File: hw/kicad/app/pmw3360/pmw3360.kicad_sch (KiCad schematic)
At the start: 2 parts, among them J2 TOP, J4 BUTTOM

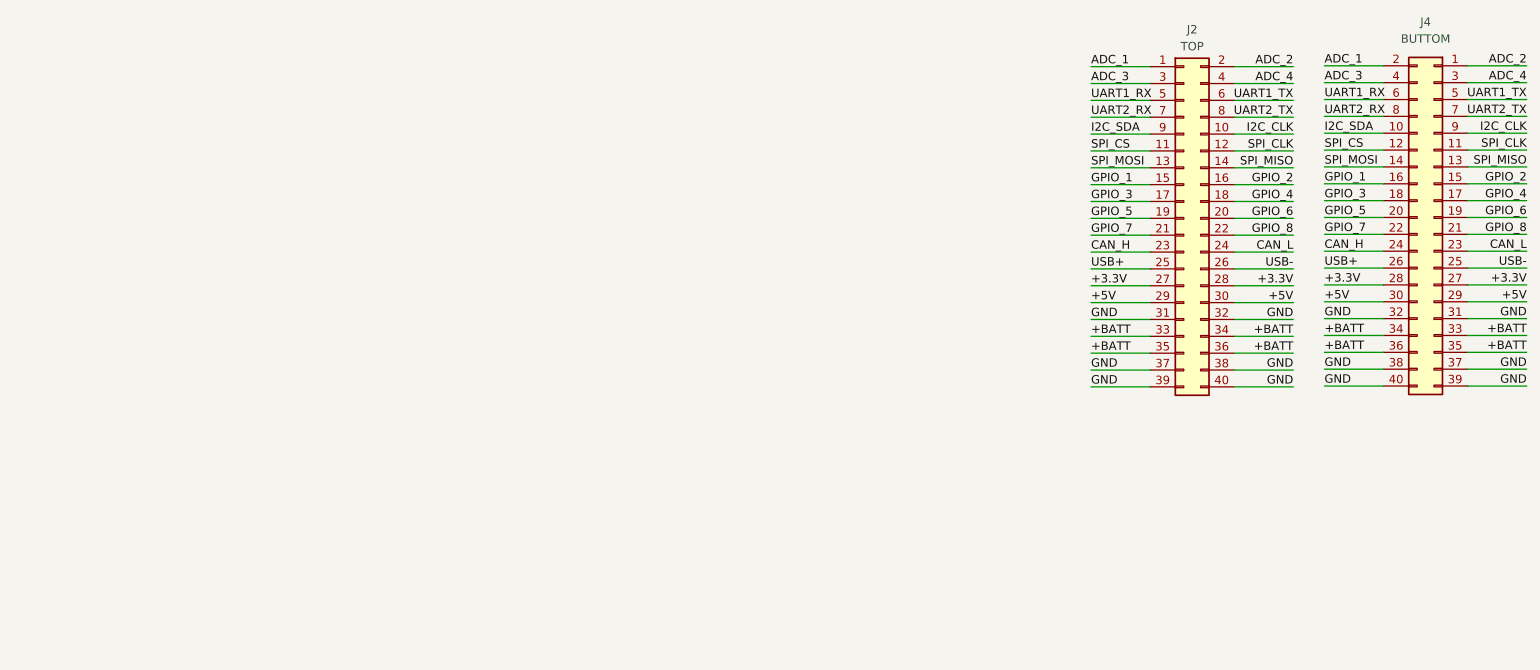
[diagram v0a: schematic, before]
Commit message: 新增陀螺仪小板子
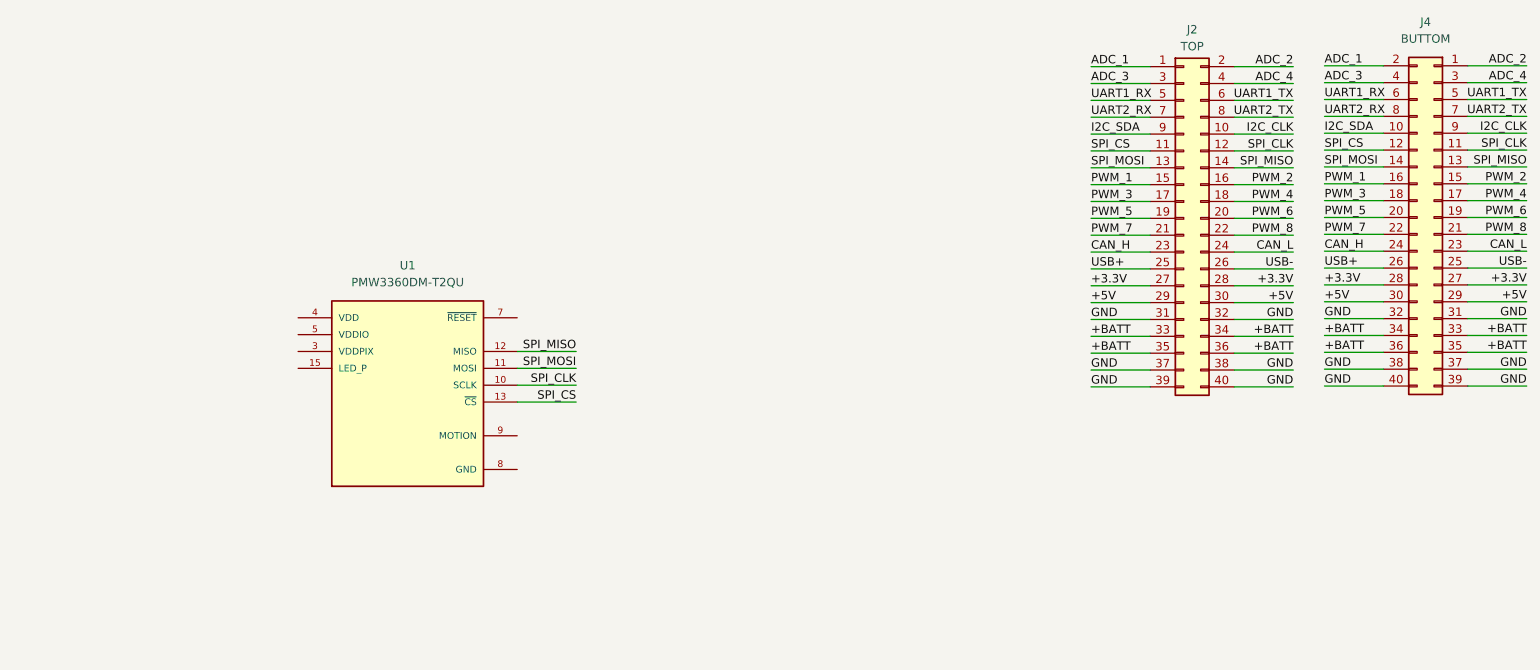
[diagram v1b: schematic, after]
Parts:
- added U1: PMW3360DM-T2QU, symbol PMW3360DM:PMW3360DM-T2QU
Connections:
- net SPI_CLK: now also U1.10 (SCLK)
- net SPI_CS: now also U1.13 (~{CS})
- net SPI_MISO: now also U1.12 (MISO)
- net SPI_MOSI: now also U1.11 (MOSI)
- net GPIO_1 renamed PWM_1
- net GPIO_2 renamed PWM_2
- net GPIO_3 renamed PWM_3
- net GPIO_4 renamed PWM_4
- net GPIO_5 renamed PWM_5
- net GPIO_6 renamed PWM_6
- net GPIO_7 renamed PWM_7
- net GPIO_8 renamed PWM_8
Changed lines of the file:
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@@
+    (stroke (width 0) (type default))
+  )
+  (wire (pts (xy 128.143 84.074) (xy 119.253 84.074))
     (stroke (width 0) (type default))
   )
@@
     (stroke (width 0) (type default))
   )
+  (wire (pts (xy 128.143 89.154) (xy 119.253 89.154))
+    (stroke (width 0) (type default))
+  )
   (wire (pts (xy 271.399 56.261) (xy 262.509 56.261))
     (stroke (width 0) (type default))
   )
+  (wire (pts (xy 128.143 91.694) (xy 119.253 91.694))
+    (stroke (width 0) (type default))
+  )
   (wire (pts (xy 240.919 76.581) (xy 249.809 76.581))
     (stroke (width 0) (type default))
@@
     (stroke (width 0) (type default))
   )
+  (wire (pts (xy 128.143 86.614) (xy 119.253 86.614))
+    (stroke (width 0) (type default))
+  )
   (wire (pts (xy 240.919 89.281) (xy 249.809 89.281))
     (stroke (width 0) (type default))
@@
     (effects (font (size 1.27 1.27)) (justify right bottom))
   )
+  (label "SPI_MISO" (at 128.143 84.074 180) (fields_autoplaced)
+    (effects (font (size 1.27 1.27)) (justify right bottom))
+  )
   (label "I2C_SDA" (at 205.74 51.308 0) (fields_autoplaced)
     (effects (font (size 1.27 1.27)) (justify left bottom))
   )
-  (label "GPIO_5" (at 240.919 63.881 0) (fields_autoplaced)
-    (effects (font (size 1.27 1.27)) (justify left bottom))
-  )
-  (label "GPIO_3" (at 240.919 61.341 0) (fields_autoplaced)
+  (label "PWM_5" (at 240.919 63.881 0) (fields_autoplaced)
+    (effects (font (size 1.27 1.27)) (justify left bottom))
+  )
+  (label "PWM_3" (at 240.919 61.341 0) (fields_autoplaced)
     (effects (font (size 1.27 1.27)) (justify left bottom))
   )
@@
     (effects (font (size 1.27 1.27)) (justify right bottom))
   )
-  (label "GPIO_4" (at 271.399 61.341 180) (fields_autoplaced)
-    (effects (font (size 1.27 1.27)) (justify right bottom))
-  )
-  (label "GPIO_3" (at 205.74 61.468 0) (fields_autoplaced)
+  (label "PWM_4" (at 271.399 61.341 180) (fields_autoplaced)
+    (effects (font (size 1.27 1.27)) (justify right bottom))
+  )
+  (label "PWM_3" (at 205.74 61.468 0) (fields_autoplaced)
     (effects (font (size 1.27 1.27)) (justify left bottom))
   )
@@
     (effects (font (size 1.27 1.27)) (justify left bottom))
   )
-  (label "GPIO_6" (at 271.399 63.881 180) (fields_autoplaced)
+  (label "PWM_6" (at 271.399 63.881 180) (fields_autoplaced)
     (effects (font (size 1.27 1.27)) (justify right bottom))
   )
@@
     (effects (font (size 1.27 1.27)) (justify right bottom))
   )
-  (label "GPIO_1" (at 240.919 58.801 0) (fields_autoplaced)
-    (effects (font (size 1.27 1.27)) (justify left bottom))
-  )
-  (label "GPIO_2" (at 271.399 58.801 180) (fields_autoplaced)
+  (label "PWM_1" (at 240.919 58.801 0) (fields_autoplaced)
+    (effects (font (size 1.27 1.27)) (justify left bottom))
+  )
+  (label "SPI_CLK" (at 128.143 89.154 180) (fields_autoplaced)
+    (effects (font (size 1.27 1.27)) (justify right bottom))
+  )
+  (label "PWM_2" (at 271.399 58.801 180) (fields_autoplaced)
     (effects (font (size 1.27 1.27)) (justify right bottom))
   )
@@
     (effects (font (size 1.27 1.27)) (justify right bottom))
   )
-  (label "GPIO_7" (at 240.919 66.421 0) (fields_autoplaced)
-    (effects (font (size 1.27 1.27)) (justify left bottom))
-  )
-  (label "GPIO_8" (at 236.22 66.548 180) (fields_autoplaced)
+  (label "PWM_7" (at 240.919 66.421 0) (fields_autoplaced)
+    (effects (font (size 1.27 1.27)) (justify left bottom))
+  )
+  (label "PWM_8" (at 236.22 66.548 180) (fields_autoplaced)
     (effects (font (size 1.27 1.27)) (justify right bottom))
   )
@@
     (effects (font (size 1.27 1.27)) (justify right bottom))
   )
-  (label "GPIO_7" (at 205.74 66.548 0) (fields_autoplaced)
+  (label "PWM_7" (at 205.74 66.548 0) (fields_autoplaced)
     (effects (font (size 1.27 1.27)) (justify left bottom))
   )
@@
     (effects (font (size 1.27 1.27)) (justify right bottom))
   )
-  (label "GPIO_6" (at 236.22 64.008 180) (fields_autoplaced)
+  (label "PWM_6" (at 236.22 64.008 180) (fields_autoplaced)
     (effects (font (size 1.27 1.27)) (justify right bottom))
   )
@@
     (effects (font (size 1.27 1.27)) (justify right bottom))
   )
-  (label "GPIO_5" (at 205.74 64.008 0) (fields_autoplaced)
-    (effects (font (size 1.27 1.27)) (justify left bottom))
-  )
-  (label "GPIO_4" (at 236.22 61.468 180) (fields_autoplaced)
-    (effects (font (size 1.27 1.27)) (justify right bottom))
-  )
-  (label "GPIO_1" (at 205.74 58.928 0) (fields_autoplaced)
+  (label "PWM_5" (at 205.74 64.008 0) (fields_autoplaced)
+    (effects (font (size 1.27 1.27)) (justify left bottom))
+  )
+  (label "SPI_CS" (at 128.143 91.694 180) (fields_autoplaced)
+    (effects (font (size 1.27 1.27)) (justify right bottom))
+  )
+  (label "PWM_4" (at 236.22 61.468 180) (fields_autoplaced)
+    (effects (font (size 1.27 1.27)) (justify right bottom))
+  )
+  (label "PWM_1" (at 205.74 58.928 0) (fields_autoplaced)
     (effects (font (size 1.27 1.27)) (justify left bottom))
   )
@@
     (effects (font (size 1.27 1.27)) (justify right bottom))
   )
-  (label "GPIO_2" (at 236.22 58.928 180) (fields_autoplaced)
+  (label "PWM_2" (at 236.22 58.928 180) (fields_autoplaced)
     (effects (font (size 1.27 1.27)) (justify right bottom))
   )
@@
     (effects (font (size 1.27 1.27)) (justify left bottom))
   )
+  (label "SPI_MOSI" (at 128.143 86.614 180) (fields_autoplaced)
+    (effects (font (size 1.27 1.27)) (justify right bottom))
+  )
   (label "GND" (at 240.919 86.741 0) (fields_autoplaced)
     (effects (font (size 1.27 1.27)) (justify left bottom))
@@
     (effects (font (size 1.27 1.27)) (justify right bottom))
   )
-  (label "GPIO_8" (at 271.399 66.421 180) (fields_autoplaced)
+  (label "PWM_8" (at 271.399 66.421 180) (fields_autoplaced)
     (effects (font (size 1.27 1.27)) (justify right bottom))
   )
@@
     (pin "9")
     (instances
-      (project "tamplate"
+      (project "pmw3360"
         (path "/988ee502-8596-4ebe-9b99-0eb76e7d156a"
           (reference "J4") (unit 1)
+        )
+      )
+    )
+  )
+  (symbol (lib_id "PMW3360DM:PMW3360DM-T2QU") (at 104.013 89.154 0) (unit 1)
+    (in_bom yes) (on_board yes) (dnp no) (fields_autoplaced)
+    (property "Reference" "U1" (at 102.743 71.12 0)
+      (effects (font (size 1.27 1.27)))
+    )
+    (property "Value" "PMW3360DM-T2QU" (at 102.743 73.66 0)
+      (effects (font (size 1.27 1.27)))
+    )
+    (property "Footprint" "" (at 104.013 89.154 0)
+      (effects (font (size 1.27 1.27)) hide)
+    )
+    (property "Datasheet" "" (at 104.013 89.154 0)
+      (effects (font (size 1.27 1.27)) hide)
+    )
+    (property "MANUFACTURER_NAME" "PixArt Imaging Inc." (at 104.013 89.154 0)
+      (effects (font (size 1.27 1.27)) (justify bottom) hide)
+    )
+    (property "MOUSER_PRICE-STOCK" "" (at 104.013 89.154 0)
+      (effects (font (size 1.27 1.27)) (justify bottom) hide)
+    )
+    (property "DESCRIPTION" "Optical gaming navigation sensor" (at 104.013 89.154 0)
+      (effects (font (size 1.27 1.27)) (justify bottom) hide)
+    )
+    (property "MOUSER_PART_NUMBER" "" (at 104.013 89.154 0)
+      (effects (font (size 1.27 1.27)) (justify bottom) hide)
+    )
+    (property "HEIGHT" "mm" (at 104.013 89.154 0)
+      (effects (font (size 1.27 1.27)) (justify bottom) hide)
+    )
+    (property "ARROW_PRICE-STOCK" "" (at 104.013 89.154 0)
+      (effects (font (size 1.27 1.27)) (justify bottom) hide)
+    )
+    (property "ARROW_PART_NUMBER" "" (at 104.013 89.154 0)
+      (effects (font (size 1.27 1.27)) (justify bottom) hide)
+    )
+    (property "MANUFACTURER_PART_NUMBER" "PMW3360DM-T2QU" (at 104.013 89.154 0)
+      (effects (font (size 1.27 1.27)) (justify bottom) hide)
+    )
+    (pin "10")
+    (pin "11")
+    (pin "12")
+    (pin "13")
+    (pin "15")
+    (pin "3")
+    (pin "4")
+    (pin "5")
+    (pin "7")
+    (pin "8")
+    (pin "9")
+    (instances
+      (project "pmw3360"
+        (path "/988ee502-8596-4ebe-9b99-0eb76e7d156a"
+          (reference "U1") (unit 1)
         )
       )
@@
     (pin "9")
     (instances
-      (project "tamplate"
+      (project "pmw3360"
         (path "/988ee502-8596-4ebe-9b99-0eb76e7d156a"
           (reference "J2") (unit 1)

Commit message: 第二次打样的整改；dc motor改成了三路 io不够做不了四路；
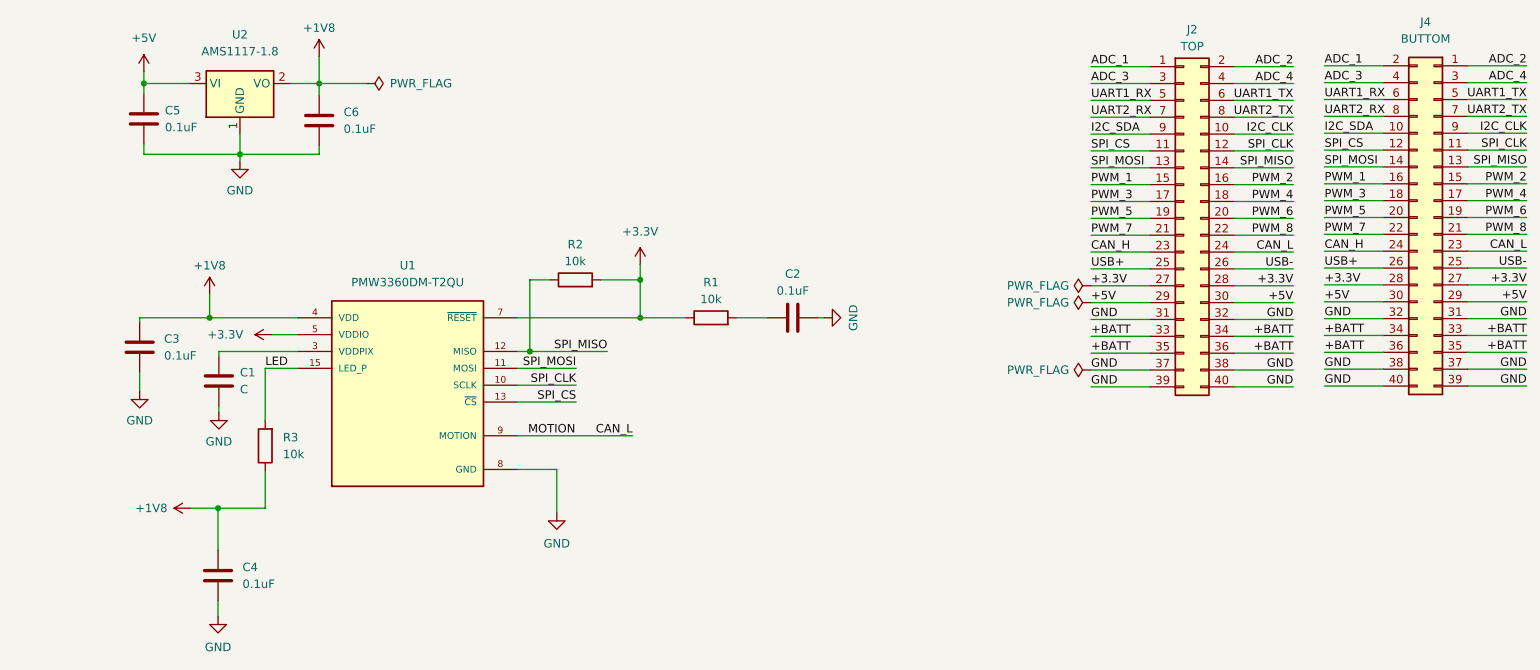
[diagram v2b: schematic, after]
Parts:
- added C1: C, Capacitor_SMD:C_0805_2012Metric, symbol Device:C
- added C2, C3, C4, C5, C6: 0.1uF, Capacitor_SMD:C_0805_2012Metric, symbol Device:C
- added R1, R2, R3: 10k, Resistor_SMD:R_0805_2012Metric, symbol Device:R
- added U2: AMS1117-1.8, Package_TO_SOT_SMD:SOT-223-3_TabPin2, symbol Regulator_Linear:AMS1117-1.8
- U1: footprint (none) -> PMW3360:PMW3360DM
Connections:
- net +3.3V: now also U1.5 (VDDIO), U1.7 (~{RESET}), R1.1, R2.2
- net +5V: now also C5.1, U2.3 (VI)
- net CAN_L: now also U1.9 (MOTION)
- net GND: now also U1.8 (GND), C1.2, C2.2, C3.2, C4.2, C5.2, C6.2, U2.1 (GND)
- net SPI_MISO: now also R2.1
- net LED: now reaches U1.15 (LED_P)
- net LED: now also R3.2
- net at U1.3 (VDDPIX): now also C1.1
- net +1V8: now reaches U1.4 (VDD)
- net +1V8: now also C3.1, C4.1, C6.1, R3.1, U2.2 (VO)
- new net: C2.1, R1.2

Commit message: 新增app板 PMW3360
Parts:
- removed J4: BUTTOM, Connector_PinHeader_1.27mm:PinHeader_2x20_P1.27mm_Vertical_SMD, symbol Connector_Generic:Conn_02x20_Odd_Even
- removed R2: 10k, Resistor_SMD:R_0805_2012Metric, symbol Device:R
- added J1: TOP, Connector_PinHeader_1.27mm:PinHeader_2x20_P1.27mm_Vertical_SMD, symbol Connector_Generic:Conn_02x20_Odd_Even
- J2: value TOP -> BUTTOM
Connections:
- net +3.3V: now also R1.2, J1.27 (Pin_27), J1.28 (Pin_28); no longer R1.1, U1.7 (~{RESET})
- net +5V: now also J1.29 (Pin_29), J1.30 (Pin_30)
- net +BATT: now also J1.33 (Pin_33), J1.34 (Pin_34), J1.35 (Pin_35), J1.36 (Pin_36)
- net ADC_1: now also J2.2 (Pin_2), J1.1 (Pin_1); no longer J2.1 (Pin_1)
- net ADC_2: now also J2.1 (Pin_1), J1.2 (Pin_2); no longer J2.2 (Pin_2)
- net ADC_3: now also J2.4 (Pin_4), J1.3 (Pin_3); no longer J2.3 (Pin_3)
- net ADC_4: now also J2.3 (Pin_3), J1.4 (Pin_4); no longer J2.4 (Pin_4)
- net GND: now also C2.1, J1.31 (Pin_31), J1.32 (Pin_32), J1.37 (Pin_37), J1.38 (Pin_38), J1.39 (Pin_39), J1.40 (Pin_40); no longer C2.2
- net I2C_CLK: now also J2.9 (Pin_9), J1.10 (Pin_10); no longer J2.10 (Pin_10)
- net I2C_SDA: now also J2.10 (Pin_10), J1.9 (Pin_9); no longer J2.9 (Pin_9)
- net SPI_CLK: now also J2.11 (Pin_11), J1.12 (Pin_12); no longer J2.12 (Pin_12)
- net SPI_CS: now also J2.12 (Pin_12), J1.11 (Pin_11); no longer J2.11 (Pin_11)
- net SPI_MISO: now also J2.13 (Pin_13), J1.14 (Pin_14); no longer J2.14 (Pin_14)
- net SPI_MOSI: now also J2.14 (Pin_14), J1.13 (Pin_13); no longer J2.13 (Pin_13)
- net CAN_H renamed GPIO_10
- net GPIO_10: now also J1.24 (Pin_24)
- net CAN_L: no longer names the net of U1.9 (MOTION)
- net CAN_L: no longer J2.24 (Pin_24)
- net PWM_1 renamed GPIO_2
- net GPIO_2: now also J1.16 (Pin_16)
- net PWM_2 renamed GPIO_1
- net GPIO_1: now also J1.15 (Pin_15)
- net PWM_3 renamed GPIO_4
- net GPIO_4: now also J1.18 (Pin_18)
- net PWM_4 renamed GPIO_3
- net GPIO_3: now also J1.17 (Pin_17)
- net PWM_5 renamed GPIO_6
- net GPIO_6: now also J1.20 (Pin_20)
- net PWM_6 renamed GPIO_5
- net GPIO_5: now also J1.19 (Pin_19)
- net PWM_7 renamed GPIO_8
- net GPIO_8: now also J1.22 (Pin_22)
- net PWM_8 renamed GPIO_7
- net GPIO_7: now also J1.21 (Pin_21)
- net UART1_RX renamed UART1_Tx
- net UART1_Tx: now also J1.6 (Pin_6)
- net UART1_TX renamed UART1_Rx
- net UART1_Rx: now also J1.5 (Pin_5)
- net UART2_RX renamed UART2_Tx
- net UART2_Tx: now also J1.8 (Pin_8)
- net UART2_TX renamed UART2_Rx
- net UART2_Rx: now also J1.7 (Pin_7)
- net USB+ renamed GPIO_12
- net GPIO_12: now also J1.26 (Pin_26)
- net USB- renamed GPIO_11
- net GPIO_11: now also J1.25 (Pin_25)
- new net: C2.2, R1.1, U1.7 (~{RESET})
- new net GPIO_9: J1.23 (Pin_23), J2.24 (Pin_24)
- no-connect marks 0 -> 1
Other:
- moved on the sheet: C1, C2, C3, C4, C5, C6, R3, U1, U2

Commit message: 更新打样资料
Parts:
- added C7: 4.7uF, Capacitor_SMD:C_1206_3216Metric, symbol Device:C
- C1: value C -> 0.1uF
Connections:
- net +1V8: no longer C4.1, R3.1
- net +3.3V: now also C4.1, R3.1
- net GND: now also C7.2
- net at C1.1, U1.3 (VDDPIX): now also C7.1
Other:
- moved on the sheet: C1, C3, C4
